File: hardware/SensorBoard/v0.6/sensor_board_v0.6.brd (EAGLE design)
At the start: 46.8 x 39.9 mm, 48 parts, among them J3 USB-MICROB, U1 ATMEGA328P, U10 CCS811, U11 RFM69HW, U2 TSL2561, U4 MPL115A, U5 FT231XS, U7 SHT31, U8 MCP1703/3.3V, U9 MCP1703CB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

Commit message: Minor trace fix
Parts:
- moved C11 0.10 mm to (25.6, 42.4)
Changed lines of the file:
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@@
 <attribute name="VALUE" x="20.2438" y="38.7604" size="0.508" layer="121" font="vector" rot="R90"/>
 </element>
-<element name="C11" library="SparkFun-Capacitors" package="0805" value="0.1uF" x="25.5524" y="42.5196" smashed="yes">
-<attribute name="MF" value="" x="25.5524" y="42.5196" size="1.778" layer="27" display="off"/>
-<attribute name="MPN" value="" x="25.5524" y="42.5196" size="1.778" layer="27" display="off"/>
-<attribute name="OC_NEWARK" value="unknown" x="25.5524" y="42.5196" size="1.778" layer="27" display="off"/>
-<attribute name="VALUE" x="25.2476" y="43.6118" size="0.508" layer="121" font="vector"/>
+<element name="C11" library="SparkFun-Capacitors" package="0805" value="0.1uF" x="25.5524" y="42.418" smashed="yes">
+<attribute name="MF" value="" x="25.5524" y="42.418" size="1.778" layer="27" display="off"/>
+<attribute name="MPN" value="" x="25.5524" y="42.418" size="1.778" layer="27" display="off"/>
+<attribute name="OC_NEWARK" value="unknown" x="25.5524" y="42.418" size="1.778" layer="27" display="off"/>
+<attribute name="VALUE" x="25.2476" y="43.5102" size="0.508" layer="121" font="vector"/>
 </element>
 <element name="U11" library="RFM69 USB Gateway" package="LOWPOWERLAB_RFM69W-MINPADS" value="RFM69HW" x="30.5308" y="37.7952" smashed="yes" rot="MR180">
@@
 <via x="15.0368" y="24.2316" extent="1-16" drill="0.254" diameter="0.127"/>
 <via x="13.208" y="45.0088" extent="1-16" drill="0.254" diameter="0.127"/>
-<via x="16.4592" y="33.9852" extent="1-16" drill="0.254" diameter="0.127"/>
+<via x="16.4084" y="34.2392" extent="1-16" drill="0.254" diameter="0.127"/>
 <via x="25.4" y="24.9936" extent="1-16" drill="0.254" diameter="0.127"/>
 <via x="27.0764" y="38.608" extent="1-16" drill="0.254" diameter="0.127"/>
@@
 <wire x1="36.6052" y1="32.7952" x2="36.576" y2="32.766" width="0.1778" layer="16"/>
 <via x="36.576" y="32.766" extent="1-16" drill="0.254" diameter="0.127"/>
-<wire x1="36.576" y1="32.766" x2="31.6484" y2="32.766" width="0.1778" layer="1"/>
-<wire x1="31.6484" y1="32.766" x2="30.6832" y2="31.8008" width="0.1778" layer="1"/>
-<wire x1="30.6832" y1="31.8008" x2="30.6832" y2="30.41" width="0.1778" layer="1"/>
+<wire x1="36.576" y1="32.766" x2="31.8008" y2="32.766" width="0.1778" layer="1"/>
+<wire x1="31.8008" y1="32.766" x2="30.6832" y2="31.6484" width="0.1778" layer="1"/>
+<wire x1="30.6832" y1="31.6484" x2="30.6832" y2="30.41" width="0.1778" layer="1"/>
 <wire x1="30.6832" y1="30.41" x2="30.677" y2="30.4038" width="0.1778" layer="1"/>
 </signal>
@@
 <contactref element="R11" pad="2"/>
 <contactref element="J3" pad="VBUS"/>
-<wire x1="20.9596" y1="42.4096" x2="22.5044" y2="42.4096" width="0.4064" layer="1"/>
-<wire x1="22.5044" y1="42.4096" x2="22.5636" y2="42.4096" width="0.4064" layer="1"/>
-<wire x1="22.5636" y1="42.4096" x2="23.876" y2="41.0972" width="0.4064" layer="1"/>
-<wire x1="23.876" y1="41.0972" x2="23.876" y2="40.016" width="0.4064" layer="1"/>
 <wire x1="30.2641" y1="36.4871" x2="30.2641" y2="39.0271" width="0.1778" layer="1"/>
 <wire x1="30.2641" y1="39.0271" x2="29.2608" y2="40.0304" width="0.1778" layer="1"/>
 <wire x1="29.2608" y1="40.0304" x2="23.8904" y2="40.0304" width="0.1778" layer="1"/>
 <wire x1="23.8904" y1="40.0304" x2="23.876" y2="40.016" width="0.1778" layer="1"/>
-<wire x1="24.6524" y1="42.5196" x2="22.6144" y2="42.5196" width="0.1778" layer="1"/>
-<wire x1="22.6144" y1="42.5196" x2="22.5044" y2="42.4096" width="0.1778" layer="1"/>
+<wire x1="20.9596" y1="42.4096" x2="24.644" y2="42.4096" width="0.4064" layer="1"/>
+<wire x1="24.644" y1="42.4096" x2="24.6524" y2="42.418" width="0.4064" layer="1"/>
+<wire x1="24.6524" y1="42.418" x2="24.6524" y2="41.518" width="0.4064" layer="1"/>
+<wire x1="24.6524" y1="41.518" x2="23.876" y2="40.7416" width="0.4064" layer="1"/>
+<wire x1="23.876" y1="40.7416" x2="23.876" y2="40.016" width="0.4064" layer="1"/>
 </signal>
 <signal name="N$32">

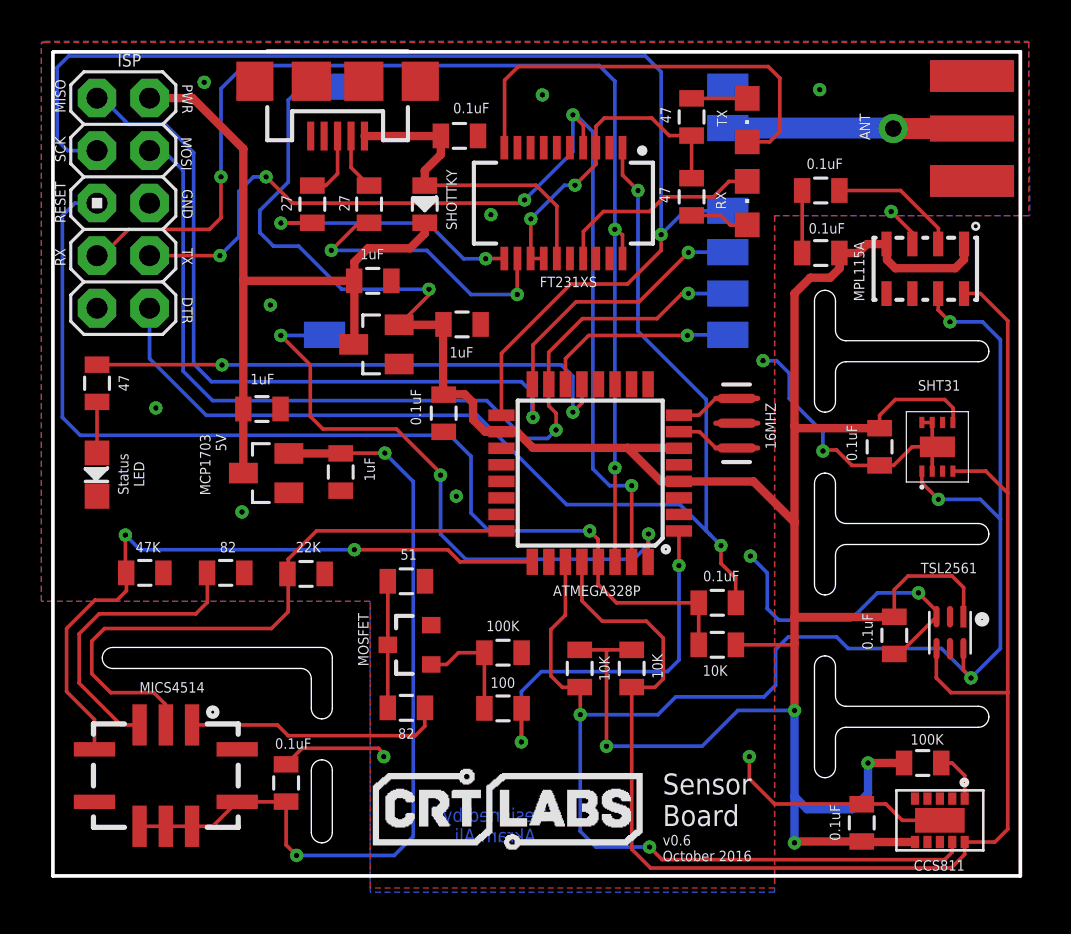
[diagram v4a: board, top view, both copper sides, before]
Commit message: Trace adjustments
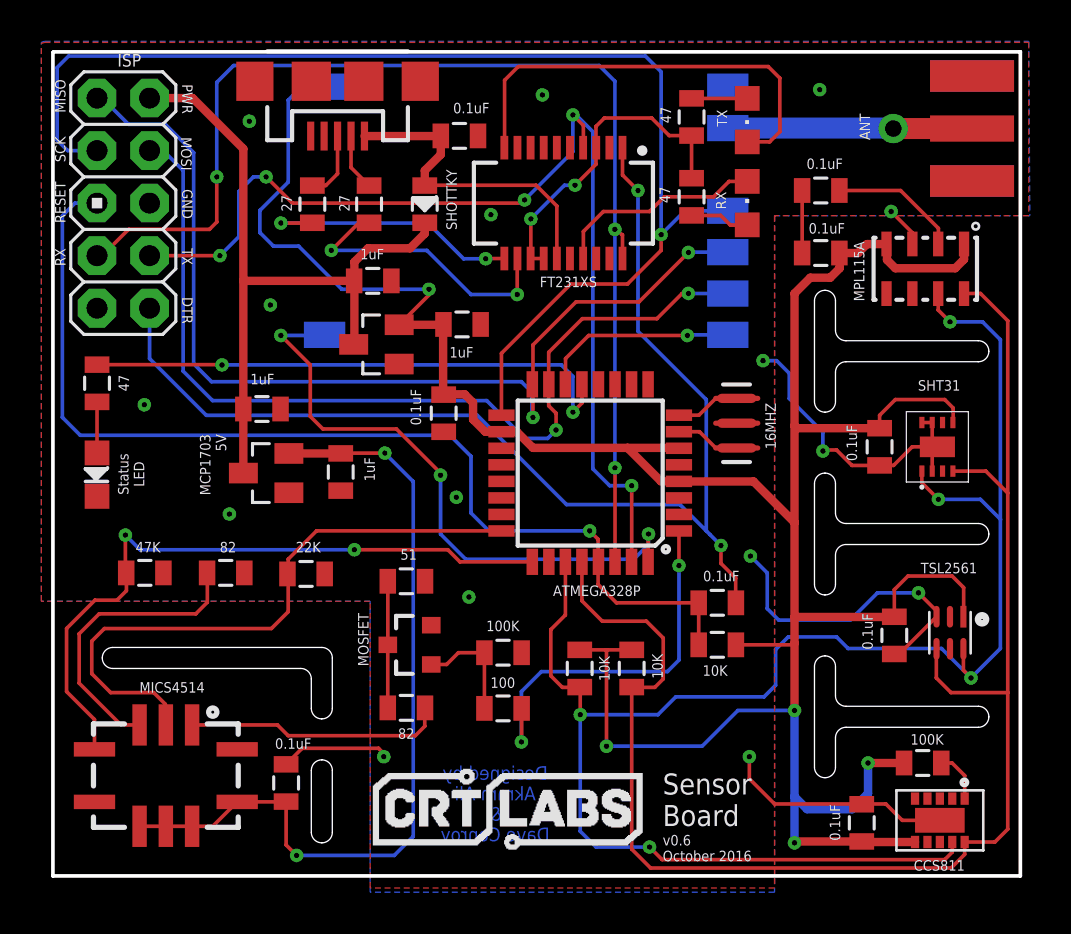
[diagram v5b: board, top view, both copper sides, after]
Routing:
- net GND: vias 15 -> 16
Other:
- board text added: "Designed by Akram Ali & Dave Conroy"
- board text removed: "Designed by Akram Ali"
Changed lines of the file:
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@@
 <wire x1="52.6796" y1="6.6294" x2="5.8928" y2="6.6294" width="0.1778" layer="20"/>
 <wire x1="5.8928" y1="6.6294" x2="5.8928" y2="46.4566" width="0.1778" layer="20"/>
-<text x="27.2796" y="9.906" size="0.6604" layer="16" font="vector" ratio="14" rot="MR180" align="bottom-center">Designed by
-Akram Ali</text>
+<text x="27.2796" y="11.938" size="0.6604" layer="16" font="vector" ratio="14" rot="MR180" align="bottom-center">Designed by
+Akram Ali
+&amp;
+Dave Conroy</text>
 <text x="35.3822" y="7.3406" size="0.508" layer="121" font="vector">v0.6
 October 2016</text>
@@
 <via x="29.5656" y="44.3992" extent="1-16" drill="0.254" diameter="0.127"/>
 <via x="46.4312" y="38.7604" extent="1-16" drill="0.254" diameter="0.127"/>
-<via x="15.0368" y="24.2316" extent="1-16" drill="0.254" diameter="0.127"/>
-<via x="13.208" y="45.0088" extent="1-16" drill="0.254" diameter="0.127"/>
+<via x="14.4272" y="24.13" extent="1-16" drill="0.254" diameter="0.127"/>
+<via x="15.3924" y="43.1292" extent="1-16" drill="0.254" diameter="0.127"/>
 <via x="16.4084" y="34.2392" extent="1-16" drill="0.254" diameter="0.127"/>
-<via x="25.4" y="24.9936" extent="1-16" drill="0.254" diameter="0.127"/>
+<via x="25.4" y="24.9428" extent="1-16" drill="0.254" diameter="0.127"/>
 <via x="27.0764" y="38.608" extent="1-16" drill="0.254" diameter="0.127"/>
 <wire x1="45.0232" y1="10.1092" x2="40.7924" y2="10.1092" width="0.1778" layer="1"/>
@@
 <wire x1="46.824" y1="17.3626" x2="48.626" y2="19.1646" width="0.1778" layer="1"/>
 <wire x1="42.1276" y1="36.7538" x2="42.1276" y2="39.7764" width="0.1778" layer="1"/>
-<via x="10.8712" y="29.2608" extent="1-16" drill="0.254" diameter="0.127"/>
+<via x="10.3124" y="29.4132" extent="1-16" drill="0.254" diameter="0.127"/>
 <wire x1="48.626" y1="19.1646" x2="48.626" y2="19.446" width="0.1778" layer="1"/>
 <wire x1="48.626" y1="19.446" x2="47.752" y2="20.32" width="0.1778" layer="1"/>
@@
 <wire x1="47.4572" y1="37.1918" x2="47.4572" y2="37.7344" width="0.1778" layer="1"/>
 <wire x1="47.4572" y1="37.7344" x2="46.4312" y2="38.7604" width="0.1778" layer="1"/>
+<via x="26.0096" y="20.1168" extent="1-16" drill="0.254" diameter="0.127"/>
 </signal>
 <signal name="VCC">
@@
 <wire x1="8.2804" y1="36.6268" x2="9.5504" y2="37.8968" width="0.1778" layer="1"/>
 <wire x1="9.5504" y1="37.8968" x2="13.462" y2="37.8968" width="0.1778" layer="1"/>
-<wire x1="13.462" y1="37.8968" x2="14.0208" y2="38.4556" width="0.1778" layer="1"/>
-<wire x1="14.0208" y1="38.4556" x2="14.0208" y2="40.4368" width="0.1778" layer="1"/>
-<via x="14.0208" y="40.4368" extent="1-16" drill="0.254" diameter="0.127"/>
-<wire x1="15.1384" y1="45.8216" x2="32.3088" y2="45.8216" width="0.1778" layer="16"/>
-<wire x1="15.1384" y1="45.8216" x2="14.0208" y2="44.704" width="0.1778" layer="16"/>
-<wire x1="14.0208" y1="44.704" x2="14.0208" y2="40.4368" width="0.1778" layer="16"/>
+<via x="13.8176" y="40.4368" extent="1-16" drill="0.254" diameter="0.127"/>
+<wire x1="14.6304" y1="45.8216" x2="32.3088" y2="45.8216" width="0.1778" layer="16"/>
 <wire x1="33.0708" y1="26.3652" x2="33.0708" y2="37.8968" width="0.1778" layer="16"/>
 <wire x1="33.0708" y1="37.8968" x2="33.0708" y2="45.0596" width="0.1778" layer="16"/>
@@
 <wire x1="33.077" y1="21.8186" x2="33.077" y2="26.359" width="0.1778" layer="1"/>
 <wire x1="33.077" y1="26.359" x2="33.0708" y2="26.3652" width="0.1778" layer="1"/>
+<wire x1="14.6304" y1="45.8216" x2="13.8176" y2="45.0088" width="0.1778" layer="16"/>
+<wire x1="13.8176" y1="45.0088" x2="13.8176" y2="40.4368" width="0.1778" layer="16"/>
+<wire x1="13.8176" y1="40.4368" x2="13.8176" y2="38.2524" width="0.1778" layer="1"/>
+<wire x1="13.8176" y1="38.2524" x2="13.462" y2="37.8968" width="0.1778" layer="1"/>
 </signal>
 <signal name="TX">
